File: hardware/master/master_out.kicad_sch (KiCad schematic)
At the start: 89 parts, among them J701 MAIN OUT L, J702 MAIN OUT R, K701 G6K-2F-Y DC12, K702 G6K-2F-Y DC12, Q701 MMBT3904, U701 SSI2162, U702 NE5532, U703 THAT1646S08, U704 THAT1646S08, U705 TL072, U706 TL072, U707 LM339

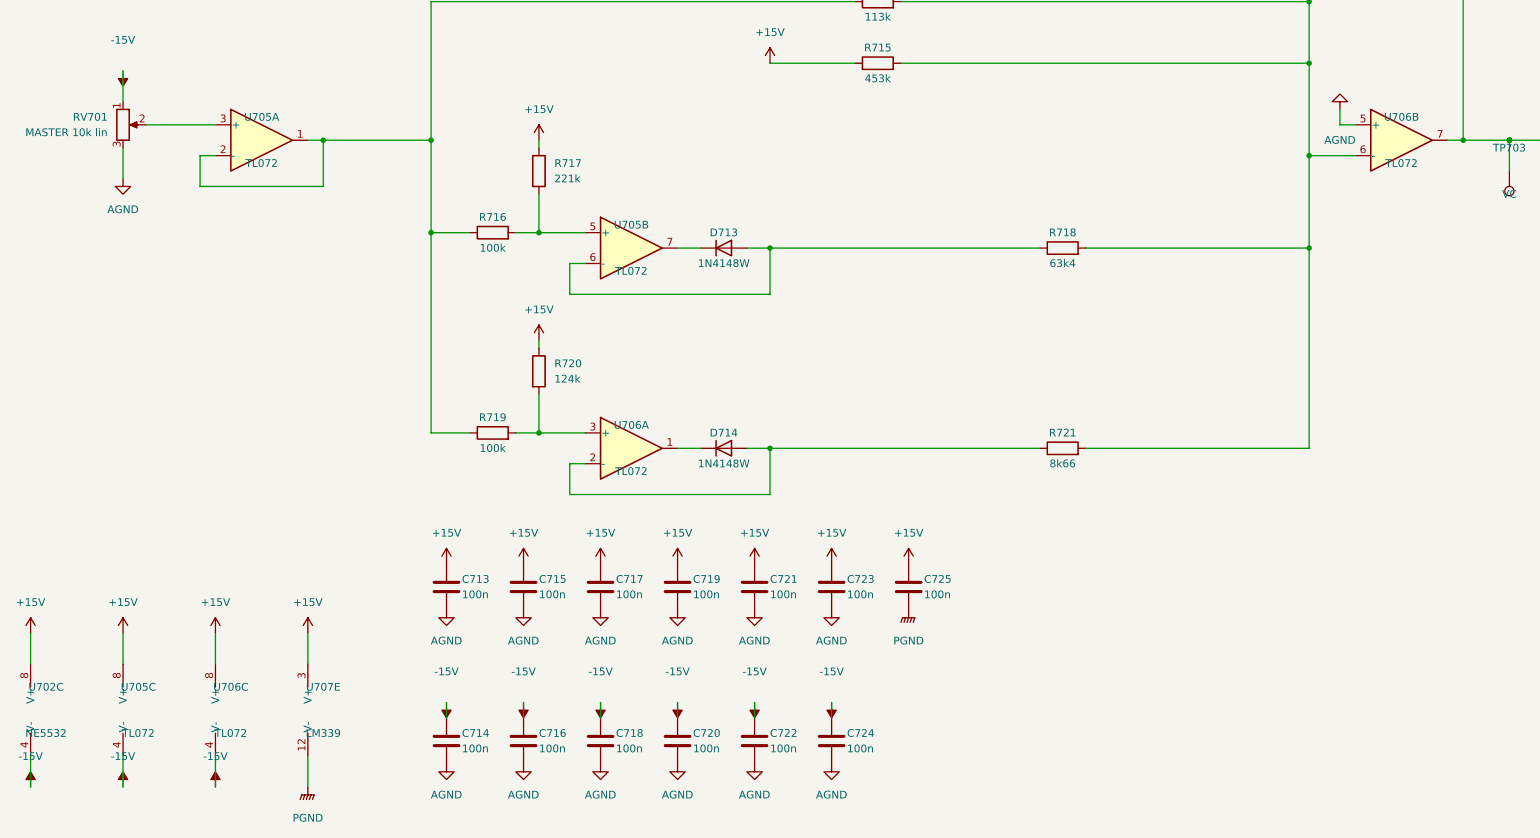
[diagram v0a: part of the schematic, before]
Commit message: Master card: draw decisions 97 and 98, OPA2171 fader-law stages (103), SC_ENV drive (104)
- AUX returns: SC_ENV into the summer's virtual earth through R232/R332 30k1,
  R233/R333 removed, summer + input on AGND (decision 97)
- Q501 emitter and button pull-downs R237/239/241, R337/339/341, R455,
  R523/525/527 to PGND (decision 98)
- U206, U306, U705 = OPA2171 for the pot buffer and control summer; superdiodes
  on the TL072s U207, U307, U706 (decision 103)
- Sidechain: DEPTH negative (R518 to -15 V), U505B follower fed back after R521,
  D504 BAT54T1G clamp to AGND (decision 104); simulation rerun with 1.7 kOhm load
- R421 on its 0603 footprint (system validation finding 3)
- Power budget, parts list, STATUS, decisions and working notes updated

Co-Authored-By: Claude Opus 5.5 <noreply@anthropic.com>
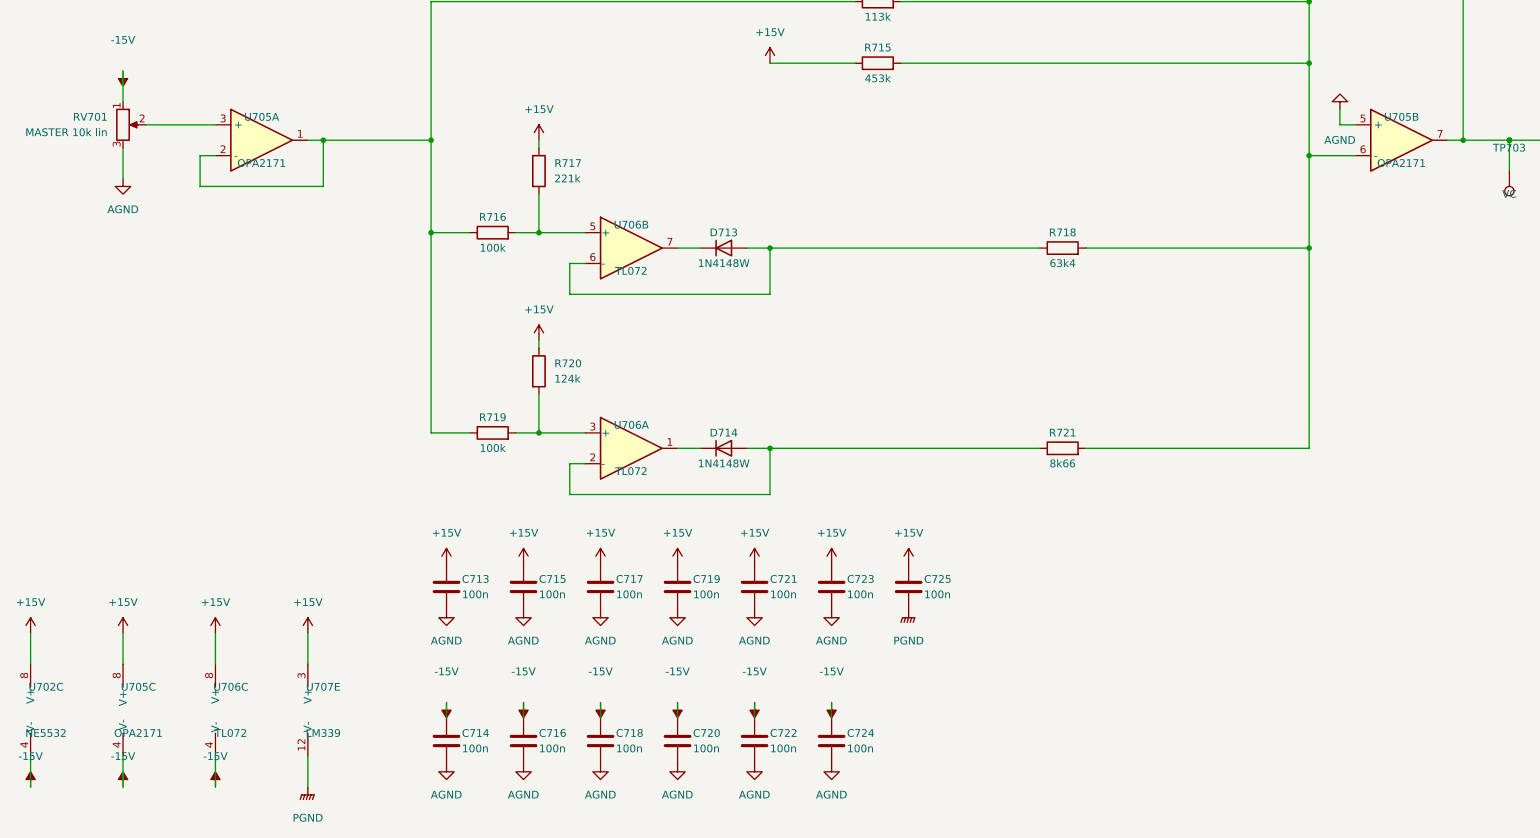
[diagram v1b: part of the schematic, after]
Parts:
- removed U705: TL072, Package_SO:SOIC-8_3.9x4.9mm_P1.27mm, symbol Amplifier_Operational:TL072
- added U705: OPA2171, Package_SO:SOIC-8_3.9x4.9mm_P1.27mm, symbol Amplifier_Operational:Opamp_Dual
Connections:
- net +15V: now also U705.8 (V+)
- net -15V: now also U705.4 (V-)
- net AGND: now also U705.5 (+); no longer U706.5 (+)
- net VC: now also U705.7; no longer U706.7
- net at R714.1, R716.1, R719.1: now also U705.1, U705.2 (-)
- net at C711.1, R714.2, R715.2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: now also U705.6 (-); no longer U706.6 (-)
- net at D713.1 (K): now also U706.7
- net at D713.2 (A), R718.1: now also U706.6 (-)
- net at R716.2, R717.2: now also U706.5 (+)
- net at RV701.2: now also U705.3 (+)

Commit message: Master card: DRV135 outputs, TL062 levers, SMD electrolytics, both raw rails watched (decisions 125-128)
/board master pre-layout session; the user delegated the open points.
- Confirms the [proposed] parts of decisions 89-94 (Q5 checked, +22 dB
  makeup kept for the breadboard, fallback R439 = 330k).
- 125: TI DRV135UA replaces the end-of-life THAT1646 (THAT memo
  2026-09-01); same SO-8 pinout, LCSC C544663.
- 126: U409, U410, U802, U804 TL072 -> TL062; superdiodes and U407 stay.
- 127: master electrolytics to SMD (decision 111 parts, 5.4 mm).
- 128: U707C watches -20V_RAW (22k6/100k), wired-OR with the +20 V trip.
- Würth fields on J101/J901, BAT54 LCSC C152458, G6K and header
  drawings checked, LCSC stock checked; budget 331/260 mA typical.
- parts.csv candidates for master pots and meter LEDs; lcsc_check.py
  handles MOhm.
ERC 0/0, all netlist checks 0 problems, reuse lint clean.

Co-Authored-By: Claude Opus 5.5 <noreply@anthropic.com>
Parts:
- added R732: 22k6, Resistor_SMD:R_0805_2012Metric, symbol Device:R
- added R733: 100k, Resistor_SMD:R_0805_2012Metric, symbol Device:R
- C701, C702, C707, C708, C709, C710: footprint Capacitor_THT:C_Radial_D5.0mm_H11.0mm_P2.00mm -> Capacitor_SMD:C_Elec_6.3x5.4; MPN (none) -> EEE-1VA100NP; Manufacturer (none) -> Panasonic; ProjectPN SX-C-003 -> SX-C-023; Supplier (none) -> Mouser; SupplierPN (none) -> 667-EEE-1VA100NP
- U703, U704: value THAT1646S08 -> DRV135UA; MPN THAT1646S08-U -> DRV135UA/2K5; Manufacturer THAT Corporation -> Texas Instruments; Note Cost-cut candidate (decision 83) -> DRV135 replaces the end-of-life THAT1646 (decision 125); sa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; ProjectPN SX-IC-014 -> SX-IC-025; Supplier Mouser -> LCSC; SupplierPN (none) -> C544663
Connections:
- net +15V: now also R732.1
- net +5V: no longer U707.10 (-)
- net PGND: no longer U707.11 (+)
- net REF: now reaches R725.2, R726.1, U707.4 (-), U707.6 (-)
- net REF: now also U707.11 (+)
- net UV_O: now reaches U707.13
- net UV_O: now also R727.1, U707.2
- new net: R732.2, R733.1, U707.10 (-)
- new net -20V_RAW: R733.2
- no-connect marks 8 -> 7

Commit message: System: cost review and cost control (decisions 132-137)
Rean NYS216 jacks with a new footprint (132), through-hole parts hand-soldered (133), E24 values owned per board (134), live-device cost principle (135), /cost with the cost-controller sub-agent, tools/costs.py and a private ledger of realized costs (136), JLCPCB fee-free parts first (137).

Co-Authored-By: Claude Opus 5.5 <noreply@anthropic.com>
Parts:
- J701, J702: footprint Connector_Audio:Jack_6.35mm_Neutrik_NMJ6HCD2_Horizontal -> syntsamix:Jack_6.35mm_Rean_NYS216_Horizontal; MPN NMJ6HCD2 -> NYS216; Manufacturer Neutrik -> Rean; ProjectPN SX-CONN-001 -> SX-CONN-015
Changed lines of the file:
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@@
 			)
 		)
-		(property "Footprint" "Connector_Audio:Jack_6.35mm_Neutrik_NMJ6HCD2_Horizontal"
+		(property "Footprint" "syntsamix:Jack_6.35mm_Rean_NYS216_Horizontal"
 			(at 269.24 147.32 0)
 			(hide yes)
@@
 			)
 		)
-		(property "ProjectPN" "SX-CONN-001"
+		(property "ProjectPN" "SX-CONN-015"
 			(at 269.24 147.32 0)
 			(hide yes)
@@
 			)
 		)
-		(property "Manufacturer" "Neutrik"
+		(property "Manufacturer" "Rean"
 			(at 269.24 147.32 0)
 			(hide yes)
@@
 			)
 		)
-		(property "MPN" "NMJ6HCD2"
+		(property "MPN" "NYS216"
 			(at 269.24 147.32 0)
 			(hide yes)
@@
 			)
 		)
-		(property "Footprint" "Connector_Audio:Jack_6.35mm_Neutrik_NMJ6HCD2_Horizontal"
+		(property "Footprint" "syntsamix:Jack_6.35mm_Rean_NYS216_Horizontal"
 			(at 269.24 45.72 0)
 			(hide yes)
@@
 			)
 		)
-		(property "ProjectPN" "SX-CONN-001"
+		(property "ProjectPN" "SX-CONN-015"
 			(at 269.24 45.72 0)
 			(hide yes)
@@
 			)
 		)
-		(property "Manufacturer" "Neutrik"
+		(property "Manufacturer" "Rean"
 			(at 269.24 45.72 0)
 			(hide yes)
@@
 			)
 		)
-		(property "MPN" "NMJ6HCD2"
+		(property "MPN" "NYS216"
 			(at 269.24 45.72 0)
 			(hide yes)

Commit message: Master card: fee-free parts and E24 values (decisions 144, 146-150)
- 144: AUX return and master fader laws on the channel's E24 pairs
- 146: meter ladder on fee-free E24 values (0.45 mA, within 0.14 dB); R732 22k + R737 560R
- 147: compressor R420/R426 E24 pairs, GR LED ladder 470k/4k3, SC LPF C503 2 x 47n C0G
  (Q 0.707, 44-478 Hz); TL072 symbols ST TL072CDT
- 148: AUX return receivers TL072 difference amplifiers (AD8273 gone from the project)
- 149: R421 plain 1k; compressor temperature compensation to the backlog
- 150: DG413, SSI2162, DRV135UA, AS3046D hand-soldered on the prototype master
  (symbol field Assembly, read by tools/costs.py); SPOF noted in the backlog
- Part swaps: button LEDs per colour, D504 BAT54W, D705-D712 1N4007W SOD-123FL,
  U641 DG411 -> DG413 with a Q601 inverter for send 1 (emitter on PGND, invariant 4)
- 70 -> 38 extended/consigned SMD types (about EUR 193 -> 105 per order);
  estimate EUR 794 / 1,074 / 1,671 for 4 / 8 / 16 channels
- Docs: STATUS, CONTINUE-FROM-HERE, ROADMAP backlog, SPEC, hardware/CLAUDE.md lessons

Co-Authored-By: Claude Opus 5.5 <noreply@anthropic.com>
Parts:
- added R734: 13k, Resistor_SMD:R_0805_2012Metric, symbol Device:R
- added R735: 150k, Resistor_SMD:R_0805_2012Metric, symbol Device:R
- added R736: 24k, Resistor_SMD:R_0805_2012Metric, symbol Device:R
- added R737: 560, Resistor_SMD:R_0805_2012Metric, symbol Device:R
- D705, D706, D707, D708, D709, D710, D711, D712: value M7 (1N4007) -> 1N4007W; footprint Diode_SMD:D_SMA -> Diode_SMD:D_SOD-123F; MPN (none) -> 1N4007W; Manufacturer (none) -> hongjiacheng; Note Phantom-power surge clamp (THAT doc 600078 Figure 8) -> Phantom-power surge clamp (THAT doc 600078 Figure 8); SOD-1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; Supplier (none) -> LCSC; SupplierPN (none) -> C18199088
- R714: value 113k -> 100k; ProjectPN SX-R-023 -> SX-R-007
- R715: value 453k -> 300k; ProjectPN SX-R-024 -> SX-R-096
- R717: value 221k -> 220k; ProjectPN SX-R-025 -> SX-R-103
- R718: value 63k4 -> 62k; ProjectPN SX-R-026 -> SX-R-102
- R720: value 124k -> 100k; ProjectPN SX-R-027 -> SX-R-007
- R721: value 8k66 -> 9k1; ProjectPN SX-R-014 -> SX-R-095
- R732: value 22k6 -> 22k; ProjectPN SX-R-071 -> SX-R-047
- U701, U703, U704: Assembly (none) -> hand (decision 150)
- U706: MPN (none) -> TL072CDT; Manufacturer Texas Instruments -> STMicroelectronics; Supplier (none) -> LCSC; SupplierPN (none) -> C6961
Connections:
- net +15V: now also R736.1, R737.1; no longer R720.1, R732.1
- net at C711.1, R718.2, R721.2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: now also R734.2, R735.2; no longer R714.2, R715.2
- new net: R732.1, R737.2
- new net: R720.1, R736.2
- new net: R714.2, R734.1
- new net: R715.2, R735.1

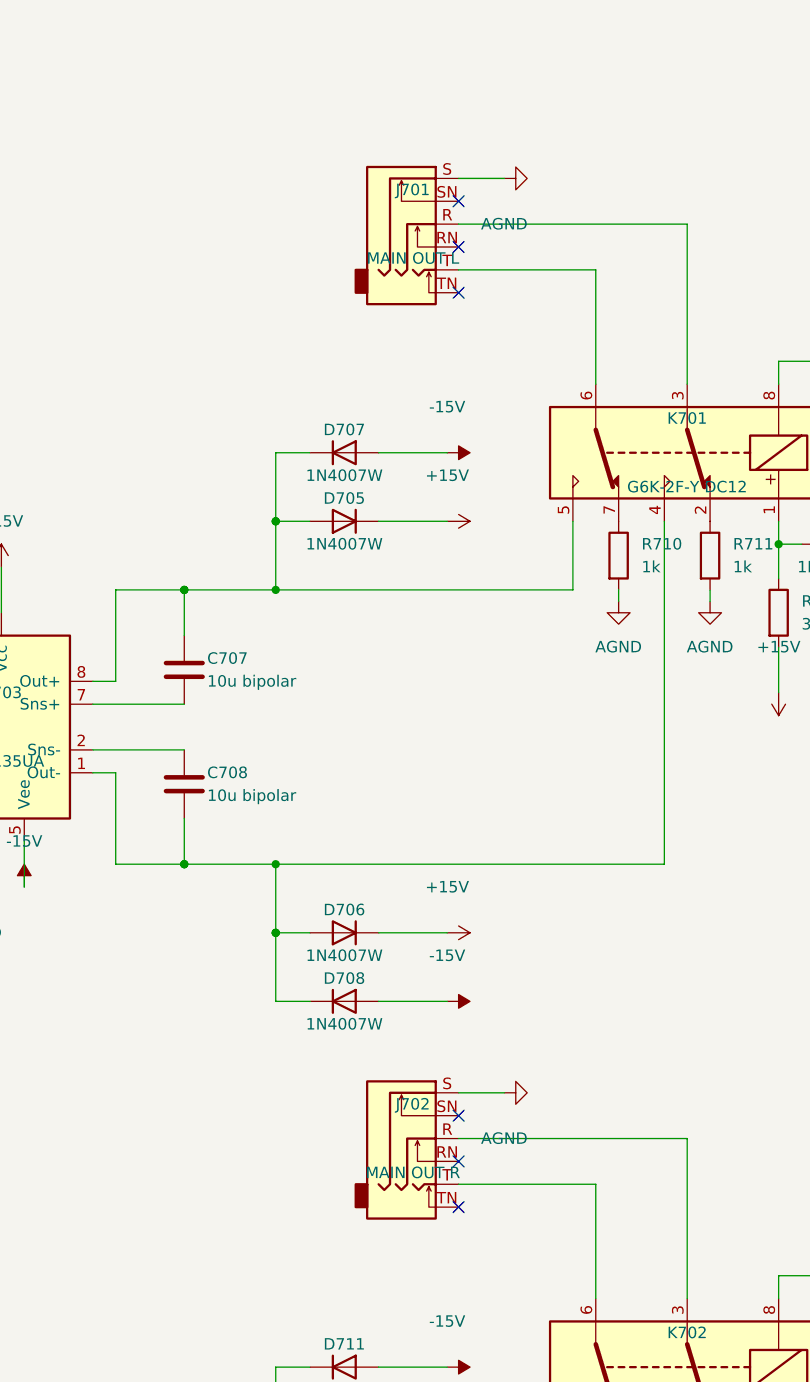
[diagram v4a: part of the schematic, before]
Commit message: Master: rear jacks on two 26-pin row-board ribbons (decision 163)
J603 (AUX sends sheet) carries main outs and both AUX sends to the
output row board; J903 (Power sheet) brings the AUX returns, SC EXT
and the ground-lift switch (pins 25/26) from the input row board.
Pairs with a ground between them; row boards hold only jacks, header
and SW901. Netlist checks 0 problems, ERC 0/0.

Co-Authored-By: Claude Opus 5.5 <noreply@anthropic.com>
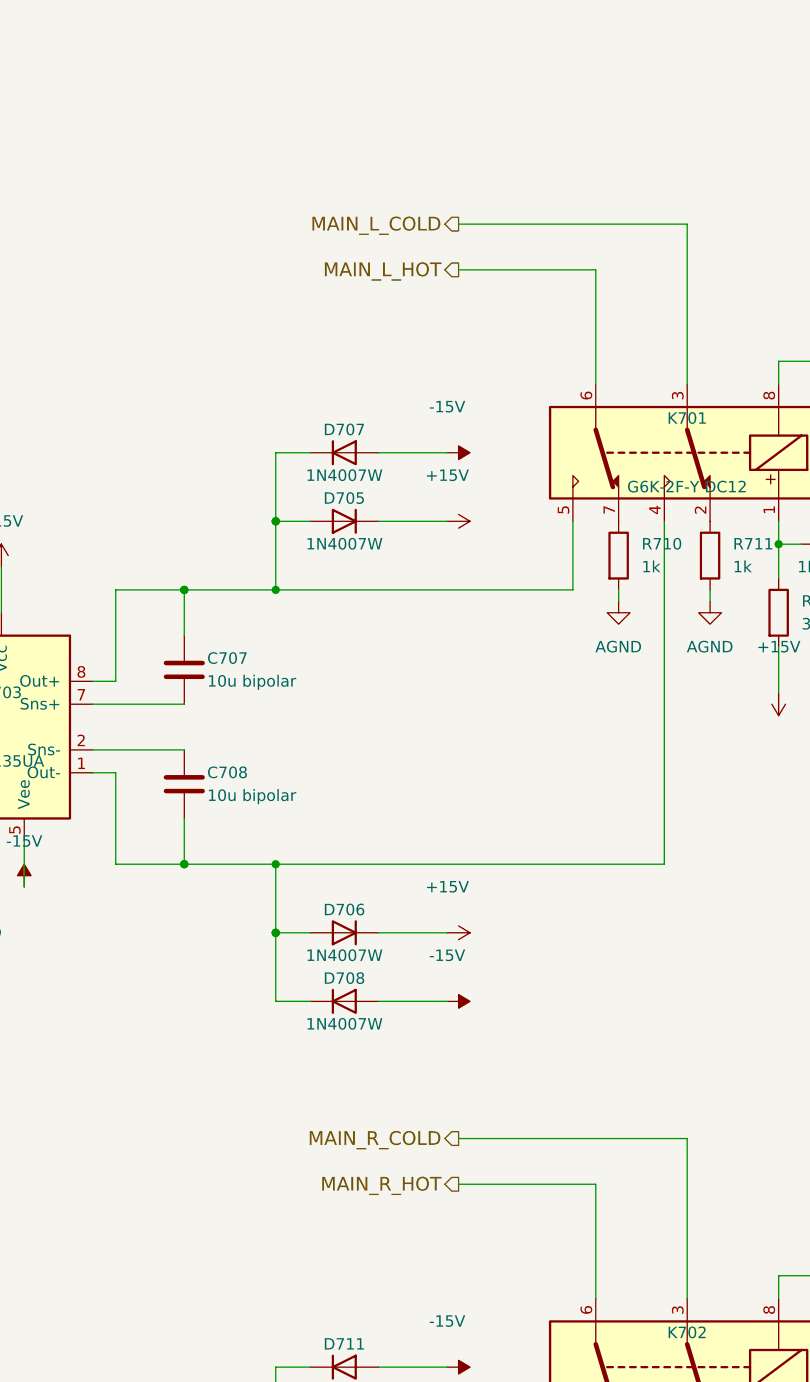
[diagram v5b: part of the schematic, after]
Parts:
- removed J701: MAIN OUT L, syntsamix:Jack_6.35mm_Rean_NYS216_Horizontal, symbol Connector_Audio:AudioJack3_Switch
- removed J702: MAIN OUT R, syntsamix:Jack_6.35mm_Rean_NYS216_Horizontal, symbol Connector_Audio:AudioJack3_Switch
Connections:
- net MAIN_L_COLD: now reaches K701.3
- net MAIN_L_HOT: now reaches K701.6
- net MAIN_R_COLD: now reaches K702.3
- net MAIN_R_HOT: now reaches K702.6
- no-connect marks 7 -> 1

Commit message: Master: back-to-back coupling pairs, ten NE5532 to TL072, Wakefield heatsinks, onsemi TO-220 regulators (decisions 172-174)
Co-Authored-By: Claude Opus 5.5 <noreply@anthropic.com>
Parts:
- removed C701, C702, C707, C708, C709, C710: 10u bipolar, Capacitor_SMD:C_Elec_6.3x5.4, symbol Device:C
- added C701, C702, C707, C708, C709, C710, C726, C727, C728, C729, C730, C731: 10u 35V, Capacitor_SMD:CP_Elec_5x5.4, symbol Device:C_Polarized
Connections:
- net MAIN_L_SUM: now also C701.1
- net MAIN_R_SUM: now also C702.1
- net at R702.1: now also C727.1
- net at D705.2 (A), D707.1 (K), K701.5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: now also C707.1
- net at U703.7 (Sns+): now also C728.1
- net at D706.2 (A), D708.1 (K), K701.4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: now also C708.1
- net at U703.2 (Sns-): now also C729.1
- net at D709.2 (A), D711.1 (K), K702.5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: now also C709.1
- net at R701.1: now also C726.1
- net at D710.2 (A), D712.1 (K), K702.4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: now also C710.1
- net at U704.2 (Sns-): now also C731.1
- net at U704.7 (Sns+): now also C730.1
- new net: C710.2, C731.2
- new net: C709.2, C730.2
- new net: C701.2, C726.2
- new net: C707.2, C728.2
- new net: C702.2, C727.2
- new net: C708.2, C729.2
